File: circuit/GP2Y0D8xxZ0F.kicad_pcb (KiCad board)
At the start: 2 copper layers, 26.8 x 24.9 mm, 13 parts, among them P1 CONN_01X04, U1 GP2Y0D81xZ0F

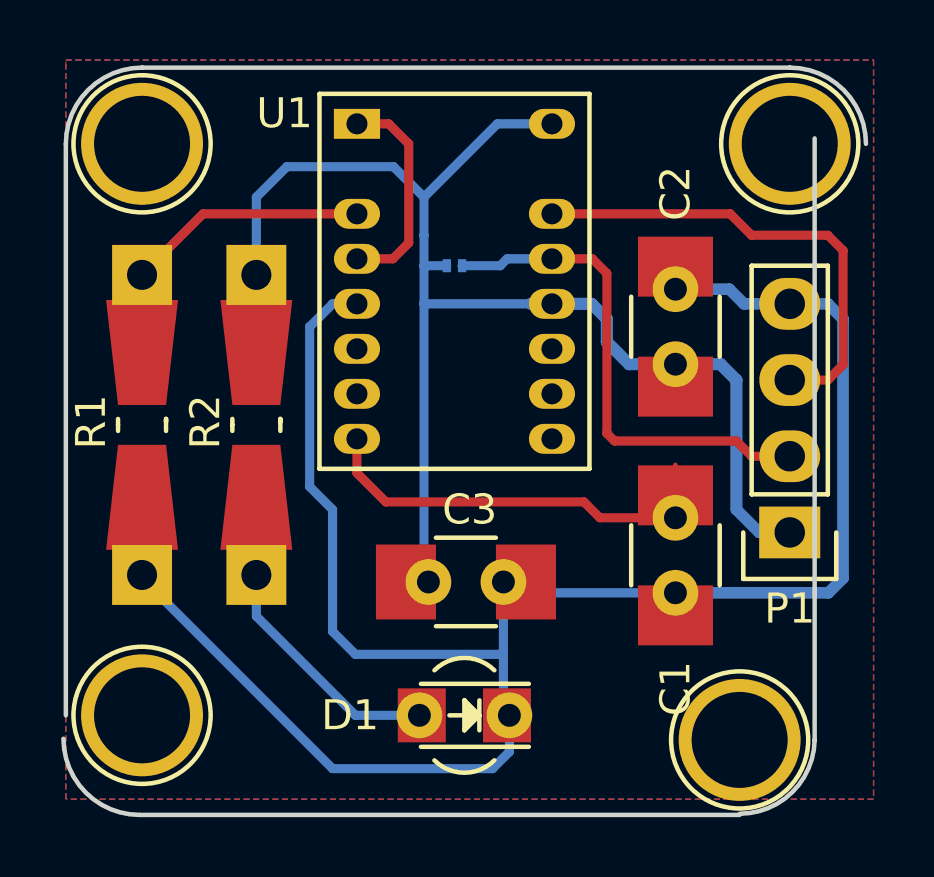
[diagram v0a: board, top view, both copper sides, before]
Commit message: Completed resizing and redraw
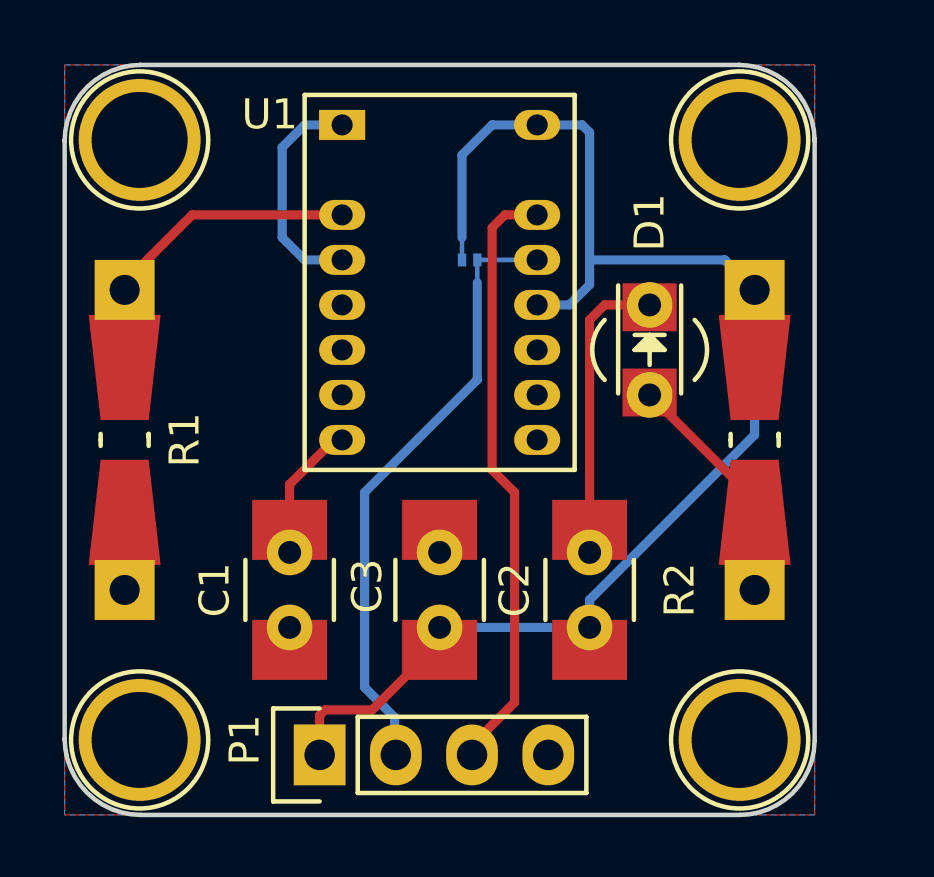
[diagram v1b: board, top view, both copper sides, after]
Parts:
- moved P1 17.3 mm to (77.0, 99.0), turned to 90 degrees
- moved R2 16.6 mm to (91.5, 88.5)
- moved D1 13.7 mm to (88.0, 85.5), turned to 270 degrees
- moved C1 12.9 mm to (76.0, 93.5)
- moved C2 9.23 mm to (86.0, 93.5)
- moved REF** 1.68 mm to (91.0, 78.5)
- moved C3 0.91 mm to (81.0, 93.5), turned to 90 degrees
- moved REF** 0.82 mm to (71.0, 98.5)
- moved R1 0.77 mm to (70.5, 88.5)
- moved JP1 0.54 mm to (82.0, 82.5)
- moved U1 0.50 mm to (81.0, 84.0)
- moved REF** 0.15 mm to (71.0, 78.5)
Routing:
- net GND: track 70.0 -> 12.0 mm
- net Net-(C1-Pad1): track 15.0 -> 4.63 mm
- net /Output: track 16.0 -> 20.1 mm
- net /Enable: track 17.6 -> 20.5 mm
- net Net-(D1-Pad2): track 10.8 -> 7.95 mm
- net VCC: track 50.8 -> 48.5 mm
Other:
- board size 26.8 x 24.9 mm -> 25 x 25 mm
